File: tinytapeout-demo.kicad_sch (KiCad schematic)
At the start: 134 parts, among them J1 Conn_01x06, J12 613012243121, J13 613012243121, J14 613012243121, J15 USB4500-03-0-A_REVA, J16 2x20_P2.54mm_Pinheader, J17 Conn_01x03, J18 2x20_P2.54mm_Pinheader, J2 Conn_01x04, J3 613012243121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

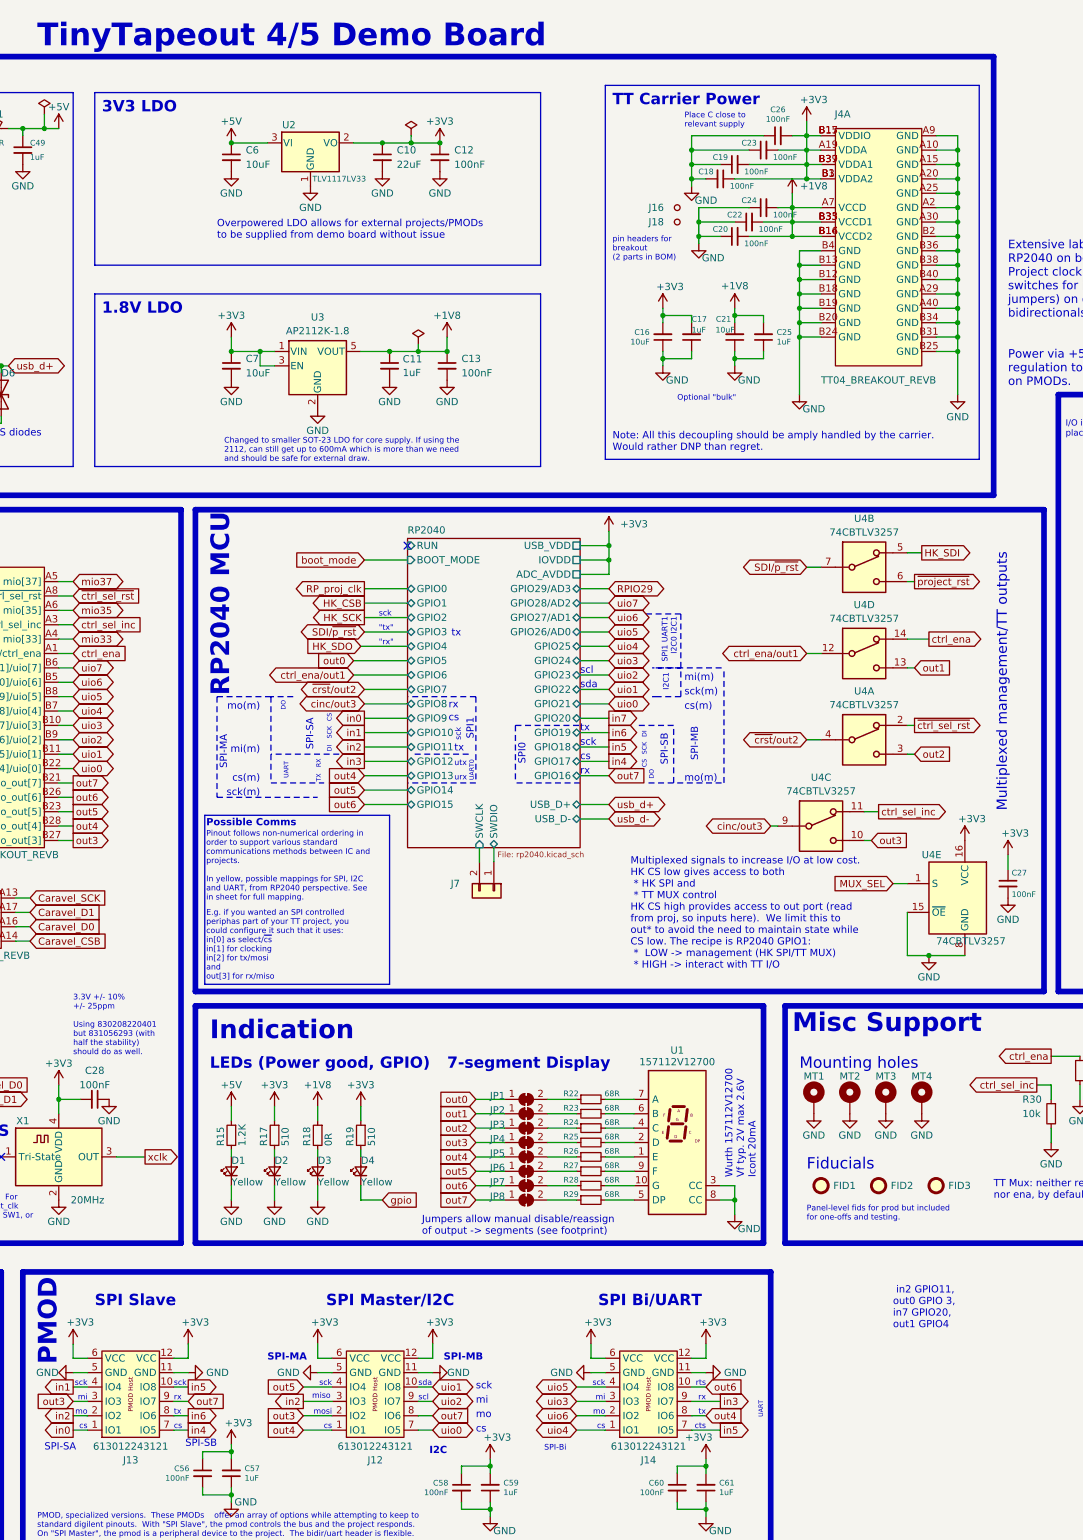
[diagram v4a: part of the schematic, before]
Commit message: reworked UART pmod, 1v8 fused and instrumentable
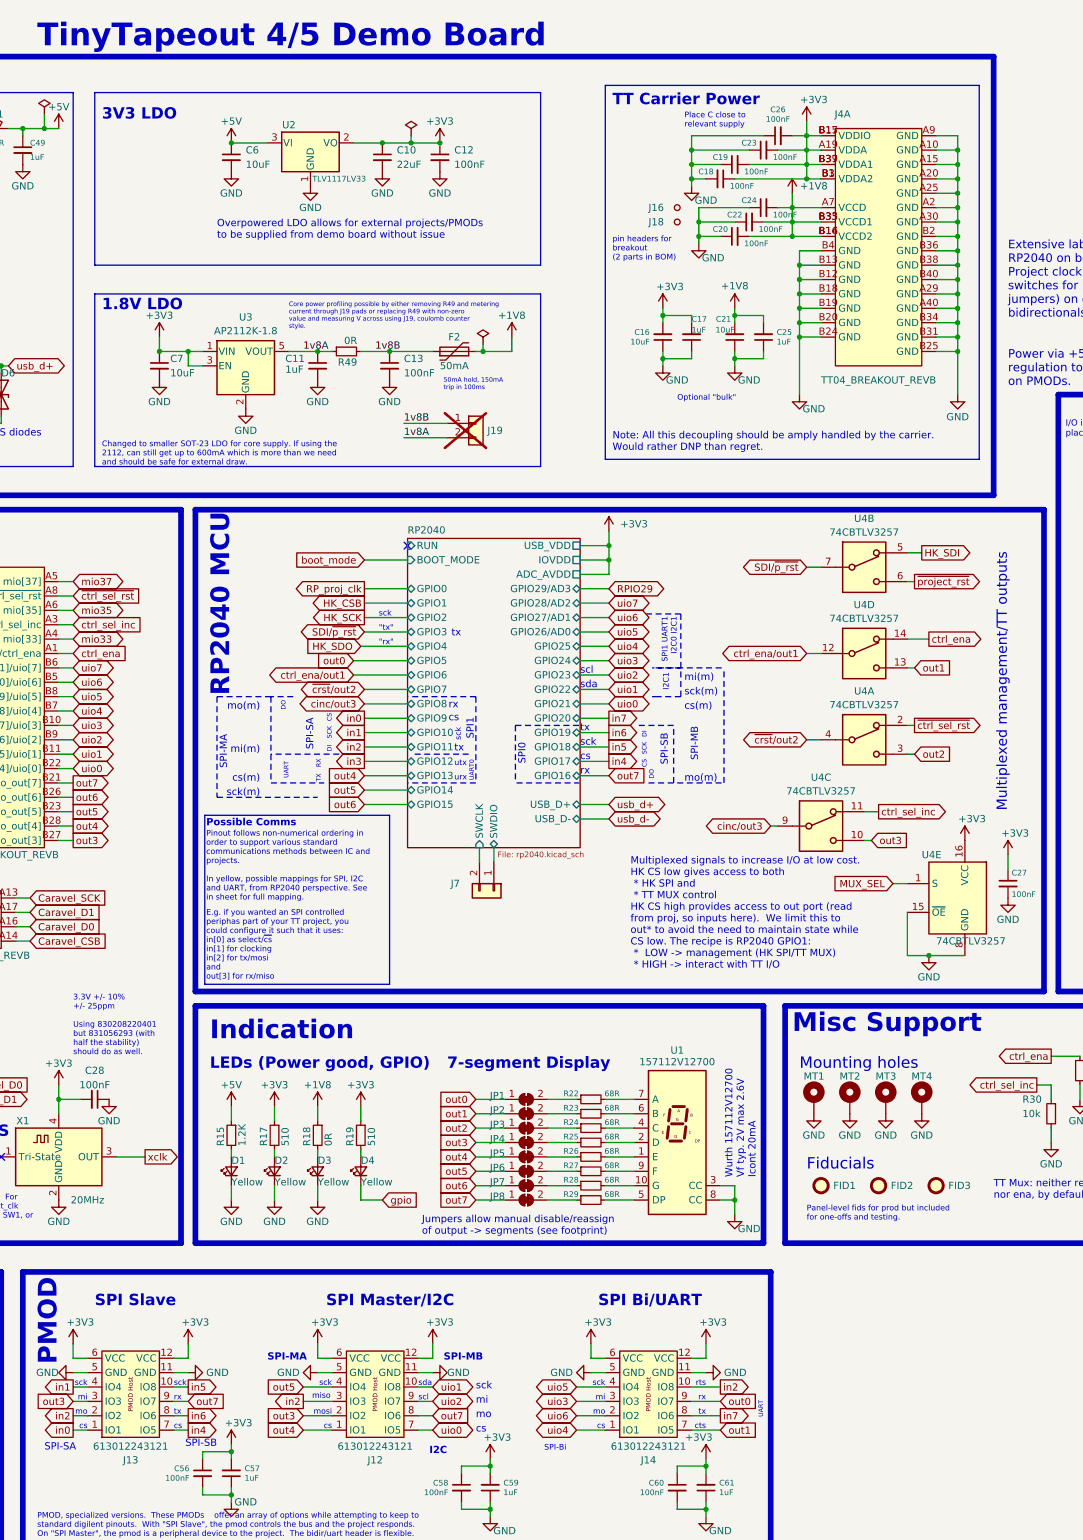
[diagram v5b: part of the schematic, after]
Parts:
- added F2: 50mA, Fuse:Fuse_0603_1608Metric, symbol Device:Polyfuse
- added J19: Conn_01x02, Connector_PinHeader_1.27mm:PinHeader_1x02_P1.27mm_Vertical, symbol Connector_Generic:Conn_01x02
- added R49: 0R, Resistor_SMD:R_0603_1608Metric, symbol Device:R_Small
- R18: footprint Resistor_SMD:R_0402_1005Metric -> Resistor_SMD:R_0603_1608Metric
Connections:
- net +1V8: now also F2.2; no longer C11.1, C13.1, U3.5 (VOUT)
- net in2: now also J14.10 (IO8)
- net in3: no longer J14.9 (IO7)
- net in5: no longer J14.7 (IO5)
- net in7: now also J14.8 (IO6)
- net out0: now also J14.9 (IO7)
- net out1: now also J14.7 (IO5)
- net out4: no longer J14.8 (IO6)
- net out6: no longer J14.10 (IO8)
- new net 1v8A: C11.1, J19.2 (Pin_2), R49.1, U3.5 (VOUT)
- new net 1v8B: C13.1, F2.1, J19.1 (Pin_1), R49.2
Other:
- note added: "50mA hold, 150mA trip in 100ms"
- note added: "Core power profiling possible by either removing R49 and metering current through J19 pads or replacing R49 with non-zero value and measuring V across using J19, coulomb counter style."
- note removed: "in2 GPIO11, out0 GPIO 3, in7 GPIO20, out1 GPIO4"
- moved on the sheet: C11, C13, C7, U3
